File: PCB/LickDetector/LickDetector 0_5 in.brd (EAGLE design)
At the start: 30 x 56 mm, 9 parts, among them IC1 74AHC1G14DBV, J1 AUDIO_JACK_3.5MM_PTH, Q1 SFH_3015_FA

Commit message: Added power and signal LEDs to Lick Detector beam break PCB
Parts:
- added PWR, SIG: (no value), led:CHIP-LED0603
- added R3, R4: (no value), resistor:R0603
- IC1: value 74AHC1G14DBV -> 74AHC1G14DCK; device 74xx-little-de:SOT23-5 -> 74xx-little-de:SC70-5
- R1, R2: device rcl:R0603 -> resistor:R0603
- moved R1 5.41 mm to (20.9, 21.9), turned to 180 degrees
- moved R2 1.69 mm to (9.50, 14.8)
- moved IC1 0.82 mm to (14.2, 16.8)
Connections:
- new net N$1: PWR.A, R3.2
- new net N$2: R4.2, SIG.A
- net GND: now also PWR.C, SIG.C
- net SIGNAL: now also R4.1
- net VCC: now also R3.1
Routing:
- net PHOTOTRANS: track 49.1 -> 54.5 mm
- net N$1: track 0.00 -> 4.55 mm
- net N$2: track 0.00 -> 2.28 mm
- net SIGNAL: track 24.5 -> 26.2 mm
- net LEDCATHODE: track 61.4 -> 60.7 mm
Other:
- board text added: "Lick Detector v1.4 7/2019 Kemere Lab"
- board text removed: "Lick Detector v1.3 6/2019 Kemere Lab"

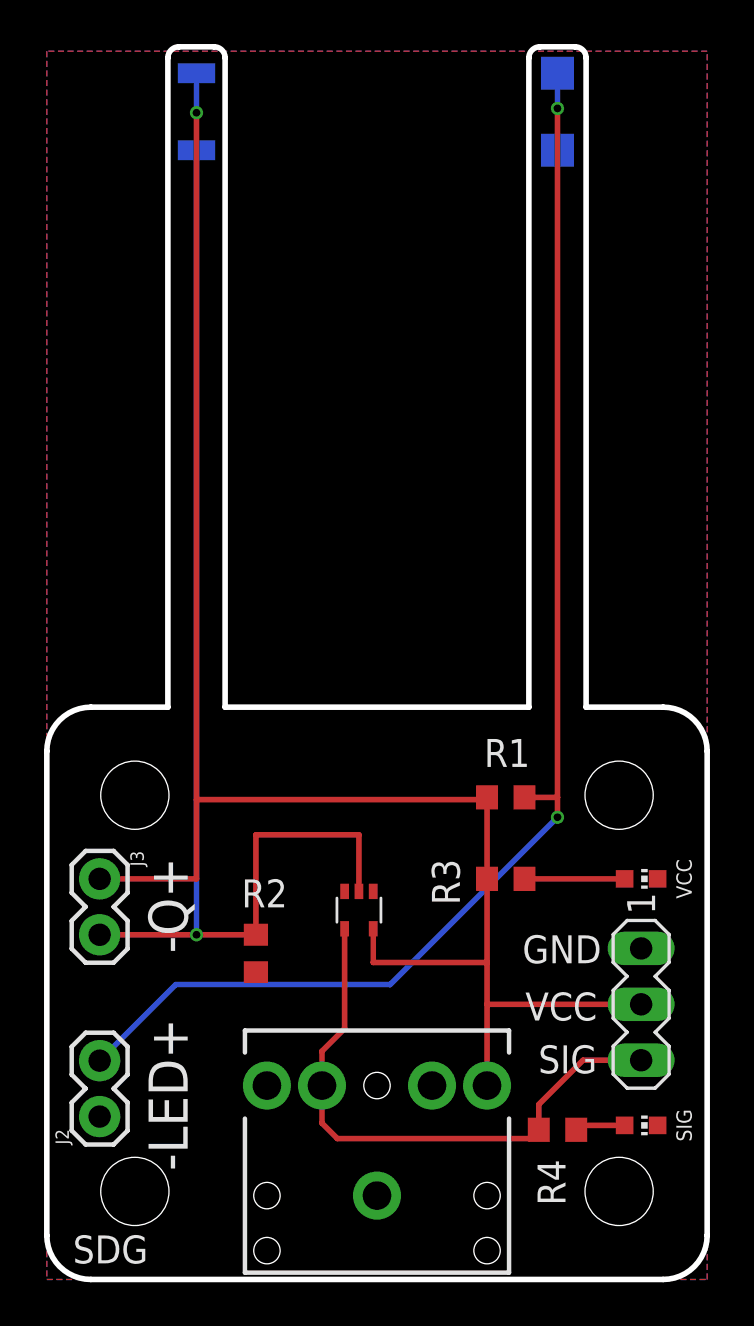
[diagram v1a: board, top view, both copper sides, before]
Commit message: Fixed bug where wrong audio jack pin was connected for signal. Also added cuttout for jack and potentiometer
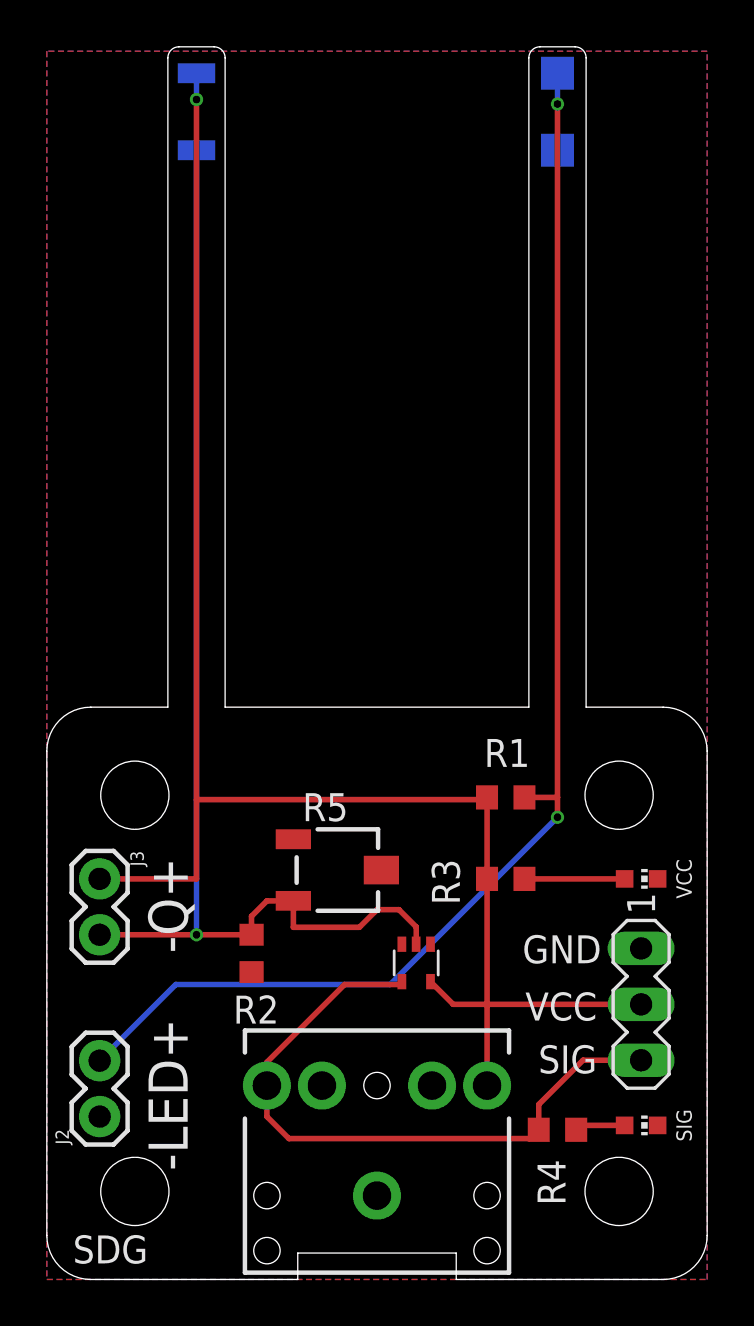
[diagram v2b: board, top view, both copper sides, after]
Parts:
- added R5: (no value), pot:3223J
- moved IC1 3.54 mm to (16.8, 14.4)
- moved R2 0.20 mm to (9.30, 14.8)
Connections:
- net GND: now also R5.2
- net PHOTOTRANS: now also R5.3
- net SIGNAL: now also J1.RING; no longer J1.RSH
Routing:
- net VCC: track 81.0 -> 77.3 mm
- net SIGNAL: track 26.2 -> 29.7 mm
- net PHOTOTRANS: track 54.5 -> 53.8 mm
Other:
- outline, holes or cut-outs redrawn
